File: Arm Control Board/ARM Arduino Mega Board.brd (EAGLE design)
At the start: 189.8 x 119.2 mm, 42 parts

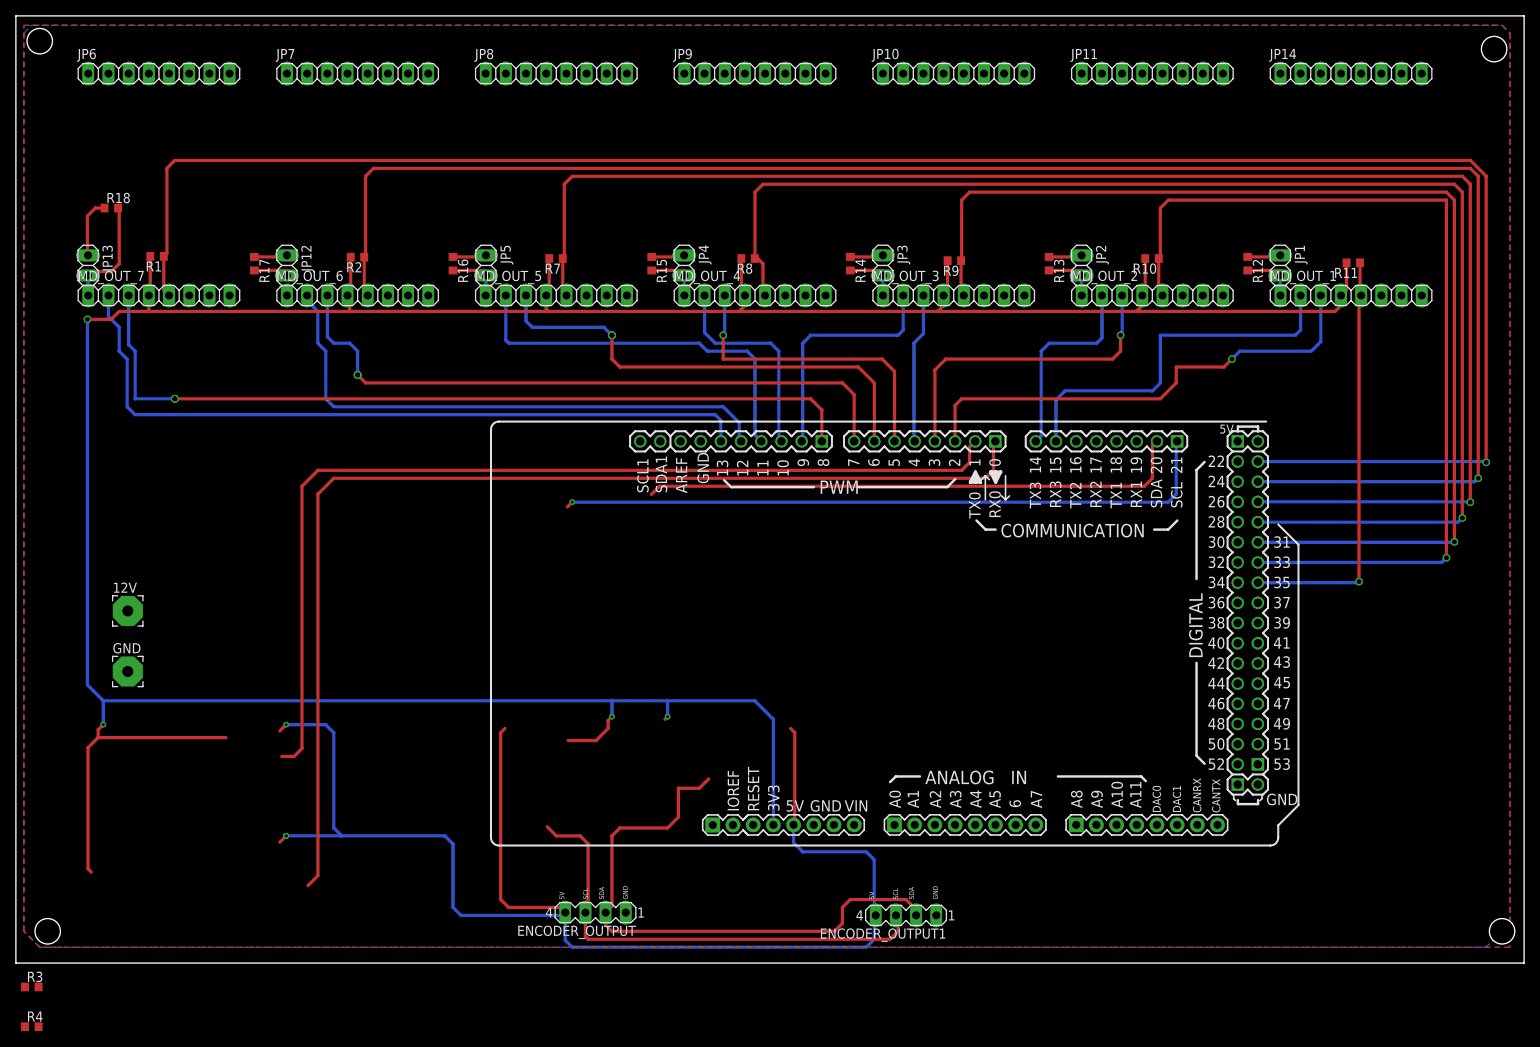
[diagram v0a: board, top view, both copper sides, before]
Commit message: Finished Layout for Relay support circuitry
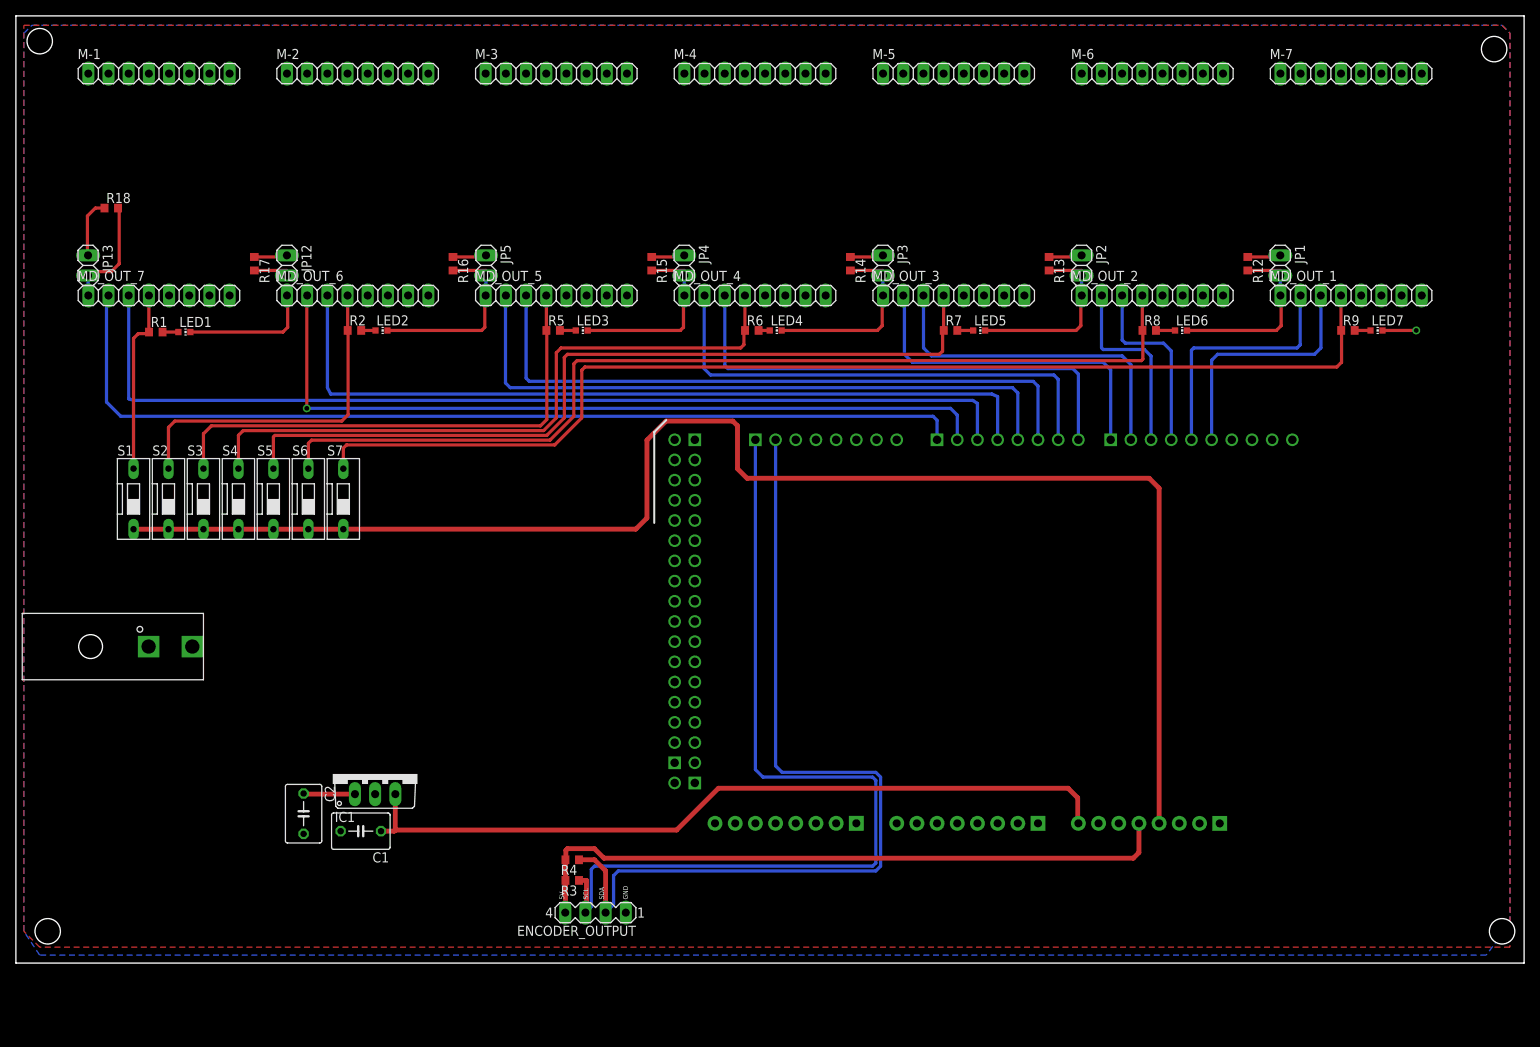
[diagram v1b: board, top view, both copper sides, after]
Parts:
- removed 12V, GND: (no value), wirepad:3,81/1,4
- removed ENCODER_OUTPUT1: (no value), con-lstb:MA04-1
- removed R10, R11: 10K, rcl:R0603
- added C1, C2: (no value), adafruit:C050-045X075
- added IC1: 7805TV, linear:TO220V
- added LED1, LED2, LED3, LED4, LED5, LED6, LED7: (no value), led:CHIP-LED0603
- added R5, R6: 25K, rcl:R0603
- added S1, S2, S3, S4, S5, S6, S7: (no value), switch-dil:DS-01
- added U$1: MEGA-FIT_RA_2, RSX:MEGA-FIT_RA_2
- R1, R2, R7, R8, R9: value 10K -> 25K
- moved ARDUINO_DUE1 119.4 mm to (175.3, 14.0), flipped to the bottom
- moved R4 71.2 mm to (66.0, 13.0), turned to 180 degrees
- moved R3 69.3 mm to (66.0, 10.4), turned to 180 degrees
- moved R8 51.3 mm to (138.6, 79.6), turned to 0 degrees
- moved R7 50.5 mm to (113.6, 79.6), turned to 0 degrees
- moved R9 50.3 mm to (163.6, 79.6), turned to 0 degrees
- moved R1 9.52 mm to (13.6, 79.4), turned to 0 degrees
- moved R2 9.22 mm to (38.6, 79.6), turned to 0 degrees
- renumbered JP10 to M-5, JP11 to M-6, JP14 to M-7, JP6 to M-1, JP7 to M-2, JP8 to M-3, JP9 to M-4
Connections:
- removed net 12V: 12V.1, ARDUINO_DUE1.VIN, M-1.7, M-1.8, M-2.7, M-2.8, M-3.7, M-3.8, M-4.7, M-4.8, M-5.7, M-5.8, M-6.7, M-6.8, M-7.7, M-7.8
- removed net 3.3V: ARDUINO_DUE1.3V3, MD_OUT_1.4, MD_OUT_2.4, MD_OUT_3.4, MD_OUT_4.4, MD_OUT_5.4, MD_OUT_6.4, MD_OUT_7.4, R1.2, R10.2, R11.2, R2.2, R7.2, R8.2, R9.2
- removed net RX: ARDUINO_DUE1.0
- removed net TX: ARDUINO_DUE1.1
- new net 3V3: ARDUINO_DUE1.3V3, S1.1, S2.1, S3.1, S4.1, S5.1, S6.1, S7.1
- new net D0: ARDUINO_DUE1.0, MD_OUT_7.2
- new net D1: ARDUINO_DUE1.1, MD_OUT_6.2
- new net N$1: LED1.A, R1.2
- new net N$28: LED3.A, R5.2
- new net N$3: LED2.A, R2.2
- new net N$30: LED4.A, R6.2
- new net N$32: LED5.A, R7.2
- new net N$34: LED6.A, R8.2
- new net N$36: LED7.A, R9.2
- new net N1: MD_OUT_2.4, R8.1, S6.2
- new net N2: MD_OUT_3.4, R7.1, S5.2
- new net N3: MD_OUT_4.4, R6.1, S4.2
- new net N4: MD_OUT_5.4, R5.1, S3.2
- new net N5: MD_OUT_6.4, R2.1, S2.2
- new net N6: MD_OUT_7.4, R1.1, S1.2
- new net N7: MD_OUT_1.4, R9.1, S7.2
- new net V+: C2.1, IC1.1, M-1.7, M-1.8, M-2.7, M-2.8, M-3.7, M-3.8, M-4.7, M-4.8, M-5.7, M-5.8, M-6.7, M-6.8, M-7.7, M-7.8, U$1.P$1
- new net VIN: ARDUINO_DUE1.VIN, C1.1, IC1.3
- net 5V: no longer ENCODER_OUTPUT1.4
- net D10: now also MD_OUT_2.2; no longer MD_OUT_4.2
- net D11: now also MD_OUT_2.3; no longer MD_OUT_5.2
- net D12: now also MD_OUT_1.2; no longer MD_OUT_6.2
- net D13: now also MD_OUT_1.3; no longer MD_OUT_7.2
- net D14: no longer MD_OUT_2.2
- net D15: no longer MD_OUT_1.2
- net D2: now also MD_OUT_7.3; no longer MD_OUT_1.3
- net D23: no longer MD_OUT_7.5, R1.1
- net D25: no longer MD_OUT_6.5, R2.1
- net D27: no longer MD_OUT_5.5, R7.1
- net D29: no longer MD_OUT_4.5, R8.1
- net D3: now also MD_OUT_6.3; no longer MD_OUT_2.3
- net D31: no longer MD_OUT_3.5, R9.1
- net D33: no longer MD_OUT_2.5, R10.1
- net D35: no longer MD_OUT_1.5, R11.1
- net D4: now also MD_OUT_5.2; no longer MD_OUT_3.3
- net D5: now also MD_OUT_5.3; no longer MD_OUT_4.3
- net D6: now also MD_OUT_4.2; no longer MD_OUT_5.3
- net D7: now also MD_OUT_4.3; no longer MD_OUT_6.3
- net D8: now also MD_OUT_3.2; no longer MD_OUT_7.3
- net D9: now also MD_OUT_3.3; no longer MD_OUT_3.2
- net GND: now also C1.2, C2.2, IC1.2, LED1.C, LED2.C, LED3.C, LED4.C, LED5.C, LED6.C, LED7.C, U$1.P$2; no longer ENCODER_OUTPUT1.1, GND.1
- net SCL_OUT: no longer ENCODER_OUTPUT1.3
- net SDA_OUT: no longer ENCODER_OUTPUT1.2
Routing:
- net 3.3V: track 404.5 -> 0.00 mm, vias 4 -> 0
- net D23: track 248.4 -> 0.00 mm, vias 1 -> 0
- net D25: track 222.0 -> 0.00 mm, vias 1 -> 0
- net D27: track 195.8 -> 0.00 mm, vias 1 -> 0
- net 3V3: track 0.00 -> 189.3 mm
- net D29: track 170.5 -> 0.00 mm, vias 1 -> 0
- net N7: track 0.00 -> 144.6 mm
- net D31: track 142.7 -> 0.00 mm, vias 1 -> 0
- net RX: track 139.8 -> 0.00 mm
- net N1: track 0.00 -> 124.5 mm
- net TX: track 124.1 -> 0.00 mm
- net D0: track 0.00 -> 121.4 mm
- net D33: track 116.7 -> 0.00 mm, vias 1 -> 0
- net N2: track 0.00 -> 104.2 mm
- net GND: track 55.3 -> 157.6 mm, vias 0 -> 1
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- added copper zone on layer 1, net V+
- removed copper zone on layer 1, net 12V
